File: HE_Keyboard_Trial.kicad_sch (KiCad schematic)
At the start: 0 parts

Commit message: Fourth Commit
changing some name to not get sued :v
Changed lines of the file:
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@@
 	)
 	(sheet
-		(at 12.7 111.76)
-		(size 121.92 41.91)
+		(at 12.7 116.84)
+		(size 121.92 44.45)
 		(fields_autoplaced yes)
 		(stroke
@@
 		)
 		(property "Sheetname" "Switches, Sensor, and Mounting"
-			(at 12.7 111.0484 0)
+			(at 12.7 116.1284 0)
 			(effects
 				(font
@@
 		)
 		(property "Sheetfile" "sensor.kicad_sch"
-			(at 12.7 154.2546 0)
+			(at 12.7 161.8746 0)
 			(effects
 				(font
@@
 	(sheet
 		(at 12.7 15.24)
-		(size 121.92 41.91)
+		(size 121.92 44.45)
 		(fields_autoplaced yes)
 		(stroke
@@
 		)
 		(property "Sheetfile" "MB.kicad_sch"
-			(at 12.7 57.7346 0)
+			(at 12.7 60.2746 0)
 			(effects
 				(font
@@
 	)
 	(sheet
-		(at 12.7 63.5)
-		(size 121.92 41.91)
+		(at 12.7 66.04)
+		(size 121.92 44.45)
 		(fields_autoplaced yes)
 		(stroke
@@
 		)
 		(property "Sheetname" "Daughter Board"
-			(at 12.7 62.7884 0)
+			(at 12.7 65.3284 0)
 			(effects
 				(font
@@
 		)
 		(property "Sheetfile" "DB.kicad_sch"
-			(at 12.7 105.9946 0)
+			(at 12.7 111.0746 0)
 			(effects
 				(font

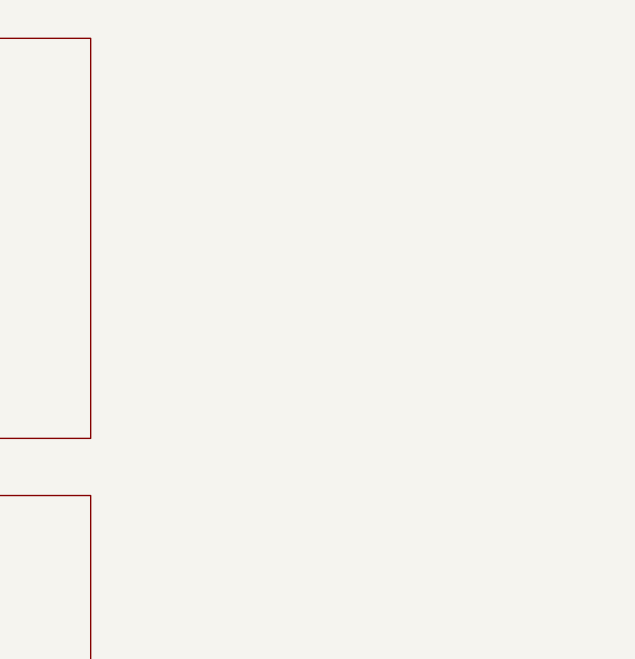
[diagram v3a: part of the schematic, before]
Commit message: 7th Commit
Adding the reduced nRF52840 dongle and some minor tweak
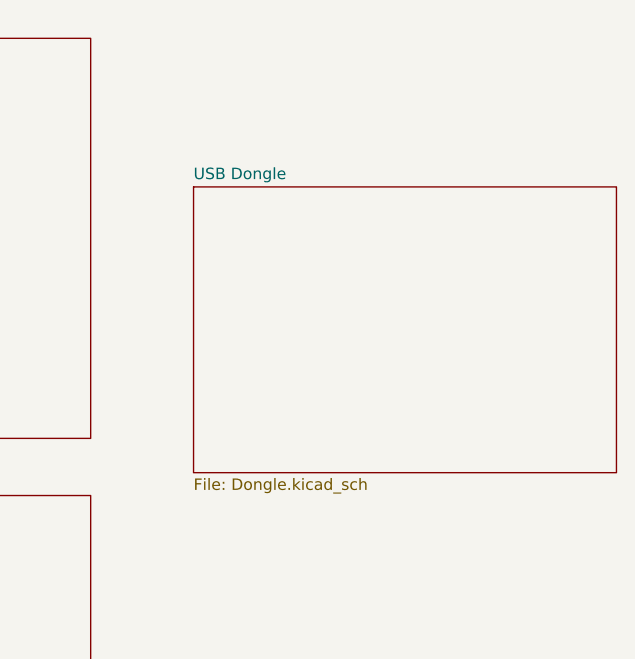
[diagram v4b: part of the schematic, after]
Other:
- added sheet USB Dongle (Dongle.kicad_sch)
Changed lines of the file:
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@@
+	)
+	(sheet
+		(at 146.05 31.75)
+		(size 46.99 31.75)
+		(fields_autoplaced yes)
+		(stroke
+			(width 0.1524)
+			(type solid)
+		)
+		(fill
+			(color 0 0 0 0.0000)
+		)
+		(property "Sheetname" "USB Dongle"
+			(at 146.05 31.0384 0)
+			(effects
+				(font
+					(size 1.27 1.27)
+				)
+				(justify left bottom)
+			)
+		)
+		(property "Sheetfile" "Dongle.kicad_sch"
+			(at 146.05 64.0846 0)
+			(effects
+				(font
+					(size 1.27 1.27)
+				)
+				(justify left top)
+			)
+		)
+		(instances
+			(project "HE_Keyboard_Trial"
+				(path "/7083d78e-5f0e-4c6d-9084-5f6f69def5a2"
+					(page "5")
+				)
+			)
+		)
 	)
 	(sheet
